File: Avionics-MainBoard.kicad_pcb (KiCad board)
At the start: 4 copper layers, 90.2 x 95.9 mm, 274 parts, among them J1 USB_C_Receptacle_USB2.0, J10 1824543, J11 1824527, J12 1824527, J13 1824527, J14 200528-0100, J15 200528-0100, J16 200528-0100, J17 1824543, J18 200528-0100, J19 200528-0100, J2 200528-0100, J3 Conn_01x06, J4 200528-0100, J5 Micro_SD_Card_Det2, J6 200528-0100, J7 U.FL-R-SMT-1, J8 Conn_01x02, J9 200528-0100, Q1 IRLML2803, Q10 MBT2222ADW1T1, Q11 MBT2222ADW1T1, Q12 MBT2222ADW1T1, Q13 MBT2222ADW1T1, Q14 MMBT2907, Q15 MMBT2907, Q16 NX3008NBKS, Q17 MBT2222ADW1T1, Q18 IRLML0030, Q19 IRF7404, Q2 MBT2222ADW1T1, Q22 NX3008NBKS, Q24 NX3008NBKS, Q26 NX3008NBKS, Q28 NX3008NBKS, Q29 MBT2222ADW1T1, Q3 MBT2222ADW1T1, Q30 MBT2222ADW1T1, Q4 NX3008NBKS, Q44 NX3008NBKS, Q46 NX3008NBKS, Q48 NX3008NBKS, Q5 MBT2222ADW1T1, Q50 NX3008NBKS, Q52 NX3008NBKS, Q6 MBT2222ADW1T1, Q7 MBT2222ADW1T1, Q8 MBT2222ADW1T1, Q9 MBT2222ADW1T1, Q99 NX3008NBKS, SW1 SW_Omron_B3FS, SW2 SW_Omron_B3FS, U1 MR25H40MDF, U12 ADM1491EBR, U14 ADM1176-1ARMZ-R7, U15 TPS7A4501DCQT, U16 ADM1176-1ARMZ-R7, U17 TPS54226PWPR, U18 ADM1176-1ARMZ-R7, U2 RP2040, U3 MAX706RESA+, U4 DS3231S, U5 BNO085, U6 USBLC6-2SC6, U7 E22-900M30S, U8 S1216V8, U9 BQ25883RGER, Y1 12MHz, Y2 32.768kHz

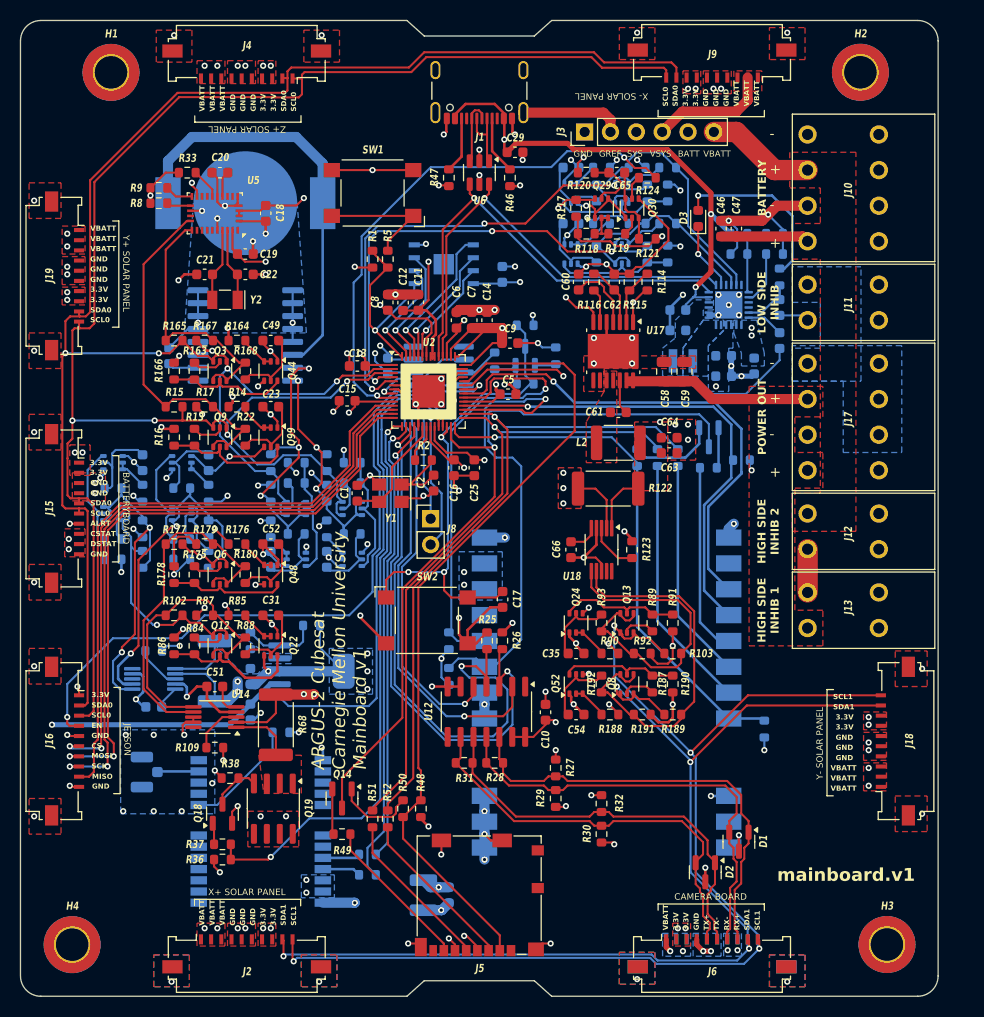
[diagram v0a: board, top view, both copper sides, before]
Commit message: Added better protection to SD card, Jetson IO, and added address breakouts to power monitors
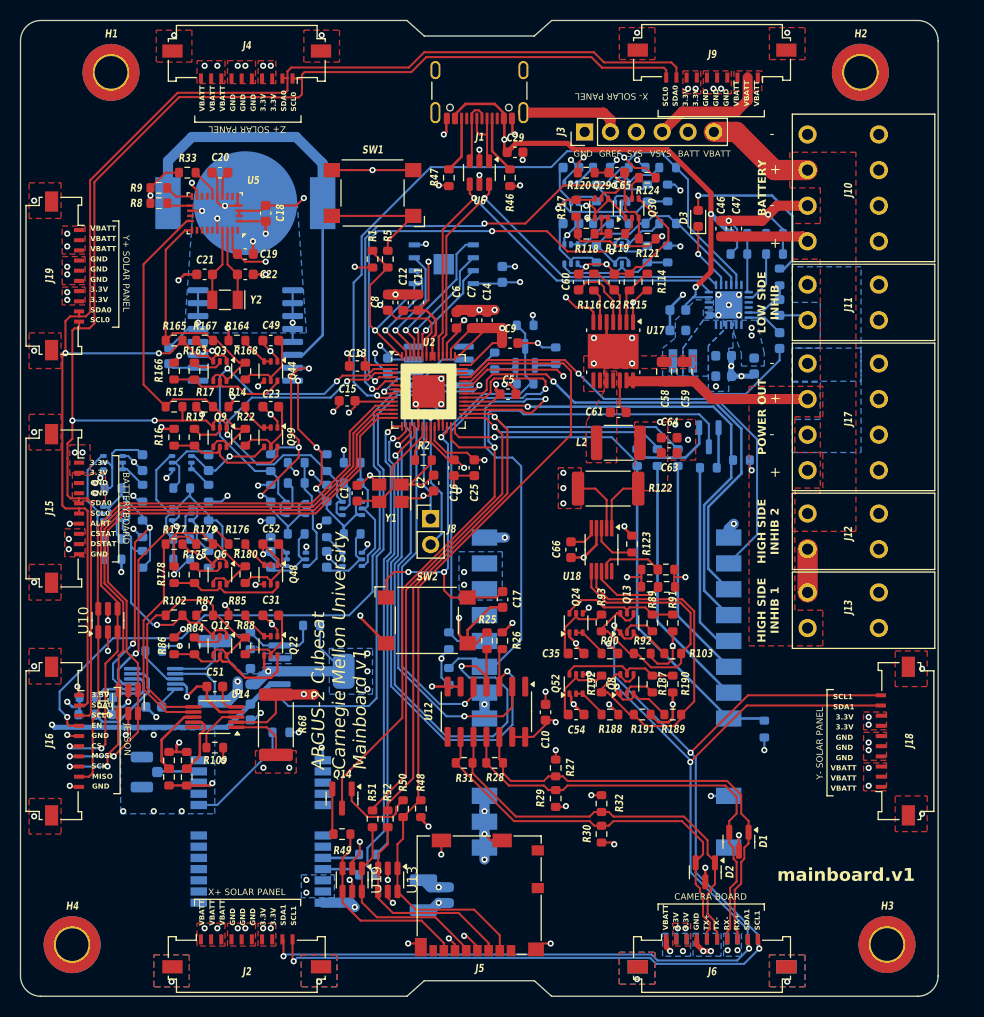
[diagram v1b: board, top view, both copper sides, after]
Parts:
- removed Q18: IRLML0030, Package_TO_SOT_SMD:SOT-23
- removed Q19: IRF7404, Package_SO:SOIC-8_3.9x4.9mm_P1.27mm
- removed R36: 10K, Resistor_SMD:R_0603_1608Metric
- removed R37: 4.7K, Resistor_SMD:R_0603_1608Metric
- removed R38: 3.3K, Resistor_SMD:R_0603_1608Metric
- removed REF**: VAL**, mainboard:board_info_block
- added R39: 0R, Resistor_SMD:R_0603_1608Metric, F.Cu at (168.4, 107.7)
- added R40: 0R, Resistor_SMD:R_0603_1608Metric, F.Cu at (166.7, 107.7)
- added R41: 0R, Resistor_SMD:R_0603_1608Metric, F.Cu at (168.3, 106.0)
- added R42: 0R, Resistor_SMD:R_0603_1608Metric, F.Cu at (166.7, 106.0)
- added R43: 0R, Resistor_SMD:R_0603_1608Metric, B.Cu at (113.2, 118.6)
- added R44: 0R, Resistor_SMD:R_0603_1608Metric, B.Cu at (111.5, 118.6)
- added R45: 0R, Resistor_SMD:R_0603_1608Metric, B.Cu at (113.1, 120.2)
- added R53: 0R, Resistor_SMD:R_0603_1608Metric, B.Cu at (111.4, 120.2)
- added R54: 0R, Resistor_SMD:R_0603_1608Metric, F.Cu at (119.5, 124.8)
- added R64: 0R, Resistor_SMD:R_0603_1608Metric, F.Cu at (119.5, 126.4)
- added R71: 0R, Resistor_SMD:R_0603_1608Metric, F.Cu at (121.2, 124.8)
- added R72: 0R, Resistor_SMD:R_0603_1608Metric, F.Cu at (121.2, 126.4)
- added U10: USBLC6-2SC6, Package_TO_SOT_SMD:SOT-23-6, F.Cu at (113.5, 111.0)
- added U11: USBLC6-2SC6, Package_TO_SOT_SMD:SOT-23-6, F.Cu at (115.5, 119.0)
- added U13: USBLC6-2SC6, Package_TO_SOT_SMD:SOT-23-6, F.Cu at (141.0, 136.5)
- added U19: USBLC6-2SC6, Package_TO_SOT_SMD:SOT-23-6, F.Cu at (137.5, 136.5)
- L2: value 3.3uH -> +3V3uH
- moved R123 0.55 mm to (165.0, 103.5)
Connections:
- J10 pad 5: GNDREF -> unconnected-(J10-Pad5)_1
- J10 pad 6: GNDREF -> unconnected-(J10-Pad6)_1
- J11 pad 3: GNDREF -> unconnected-(J11-MP-Pad3)
- J11 pad 4: GNDREF -> unconnected-(J11-MP-Pad4)
- J12 pad 3: GND -> unconnected-(J12-MP-Pad3)
- J12 pad 4: GND -> unconnected-(J12-MP-Pad4)
- J13 pad 3: GND -> unconnected-(J13-MP-Pad3)
- J13 pad 4: GND -> unconnected-(J13-MP-Pad4)
- J17 pad 5: GND -> unconnected-(J17-Pad5)
- J17 pad 6: GND -> unconnected-(J17-Pad6)_1
- R68 pad 2: Net-(U14-VCC) -> +3V3
- U14 pad 1: Net-(U14-VCC) -> +3V3
- U14 pad 8: GND -> /GPS Power/A0
- U14 pad 9: GND -> /GPS Power/A1
- U16 pad 8: unconnected-(U16-A0-Pad8) -> /LoRa Power/A0
- U16 pad 9: GND -> /LoRa Power/A1
- U18 pad 8: GND -> /Main Power/A0
- U18 pad 9: unconnected-(U18-A1-Pad9) -> /Main Power/A1
- U2 pad 39: /MCU_IO/GPS_EN -> /LoRa Power/LoRa_INT
- U7 pad 13: unconnected-(U7-DIO1-Pad13) -> /LoRa Power/LoRa_INT
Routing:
- net /MCU_IO/GPS_EN: track 70.1 -> 0.00 mm, vias 2 -> 0
- net /LoRa Power/LoRa_INT: track 0.00 -> 46.1 mm, vias 0 -> 1
- net GNDREF: track 45.8 -> 67.4 mm
- net +3V3: track 167.0 -> 186.2 mm, vias 76 -> 81
- net /LoRa Power/A1: track 0.00 -> 9.85 mm
- net /LoRa Power/A0: track 0.00 -> 7.38 mm
- net /Main Power/A0: track 0.00 -> 7.35 mm
- net /GPS Power/A0: track 0.00 -> 7.19 mm
- net GND: track 320.8 -> 327.8 mm, vias 129 -> 131
- net /Main Power/A1: track 0.00 -> 6.44 mm
- net /GPS Power/A1: track 0.00 -> 6.24 mm
- net Net-(U14-VCC): track 6.08 -> 0.00 mm
- net /SD/SD_MOSI: track 16.2 -> 21.3 mm
- net Net-(Q18-D): track 4.95 -> 0.00 mm
- net /SD/SD_CLK: track 15.7 -> 20.3 mm
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- removed copper zone on F.Cu, net Net-(U14-VCC)

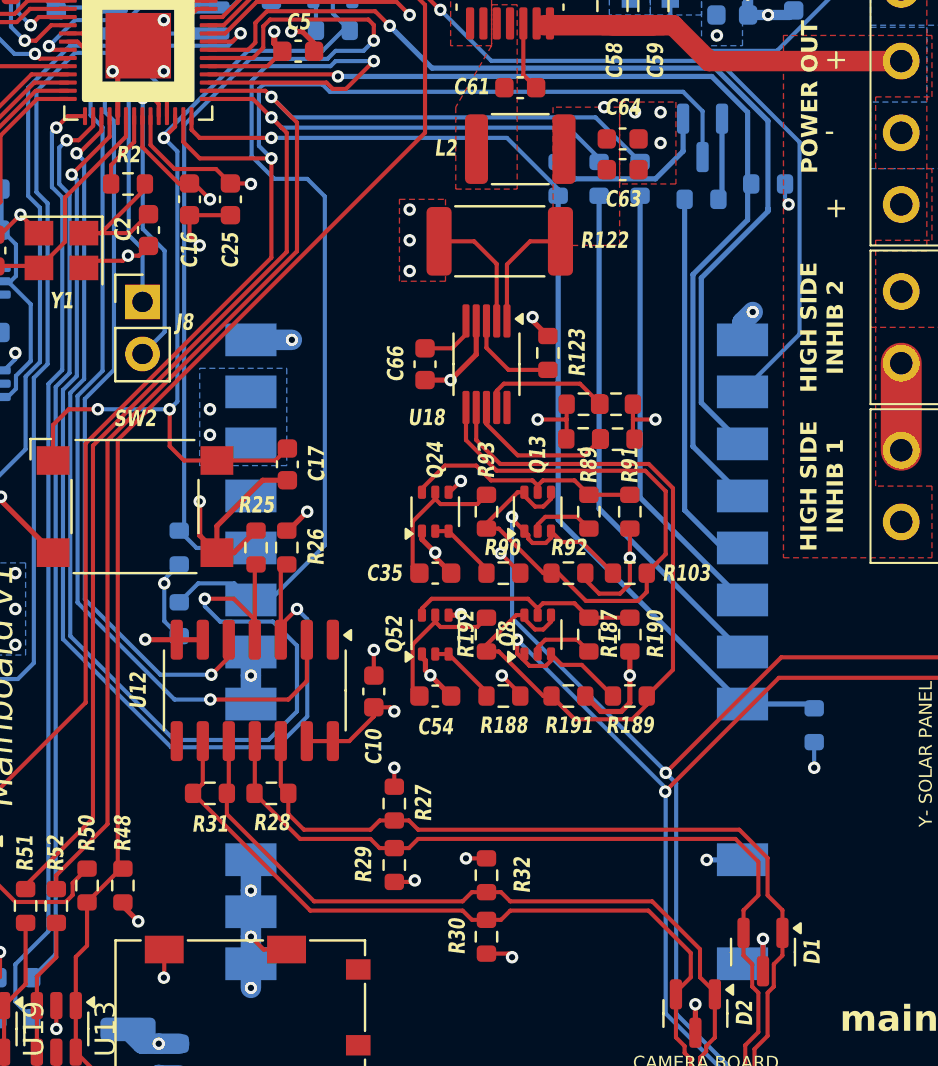
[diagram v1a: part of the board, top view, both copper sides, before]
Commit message: Added extra decoupling caps to LoRa
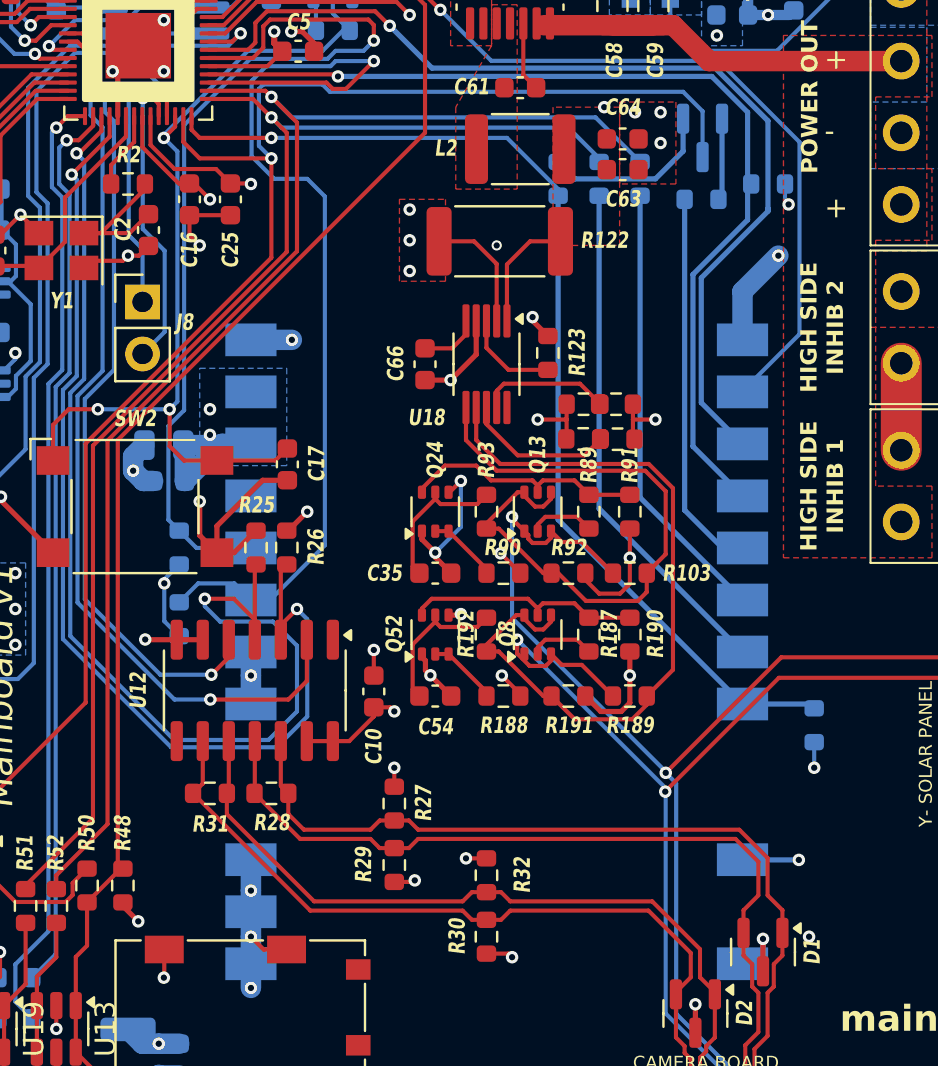
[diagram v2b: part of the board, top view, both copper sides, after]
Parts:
- added C26: 1u, Capacitor_SMD:C_0603_1608Metric, B.Cu at (146.5, 109.8)
- added C27: 10u, Capacitor_SMD:C_0805_2012Metric, B.Cu at (146.2, 108.0)
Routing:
- net GND: track 327.8 -> 419.8 mm, vias 131 -> 134
- net LoRa_VDD: track 47.9 -> 57.0 mm
- net /LoRa Power/LoRa_TX_EN: track 44.7 -> 45.5 mm

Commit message: Updated version to v2.1
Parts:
- turned H3 to 180 degrees
- turned H4 to 180 degrees
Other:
- board text added: "ARGUS-2 Cubesat Carnegie Mellon University Mainboard v2.1"
- board text added: "mainboard.v2.1"
- board text removed: "ARGUS-2 Cubesat Carnegie Mellon University Mainboard v1"
- board text removed: "mainboard.v1"

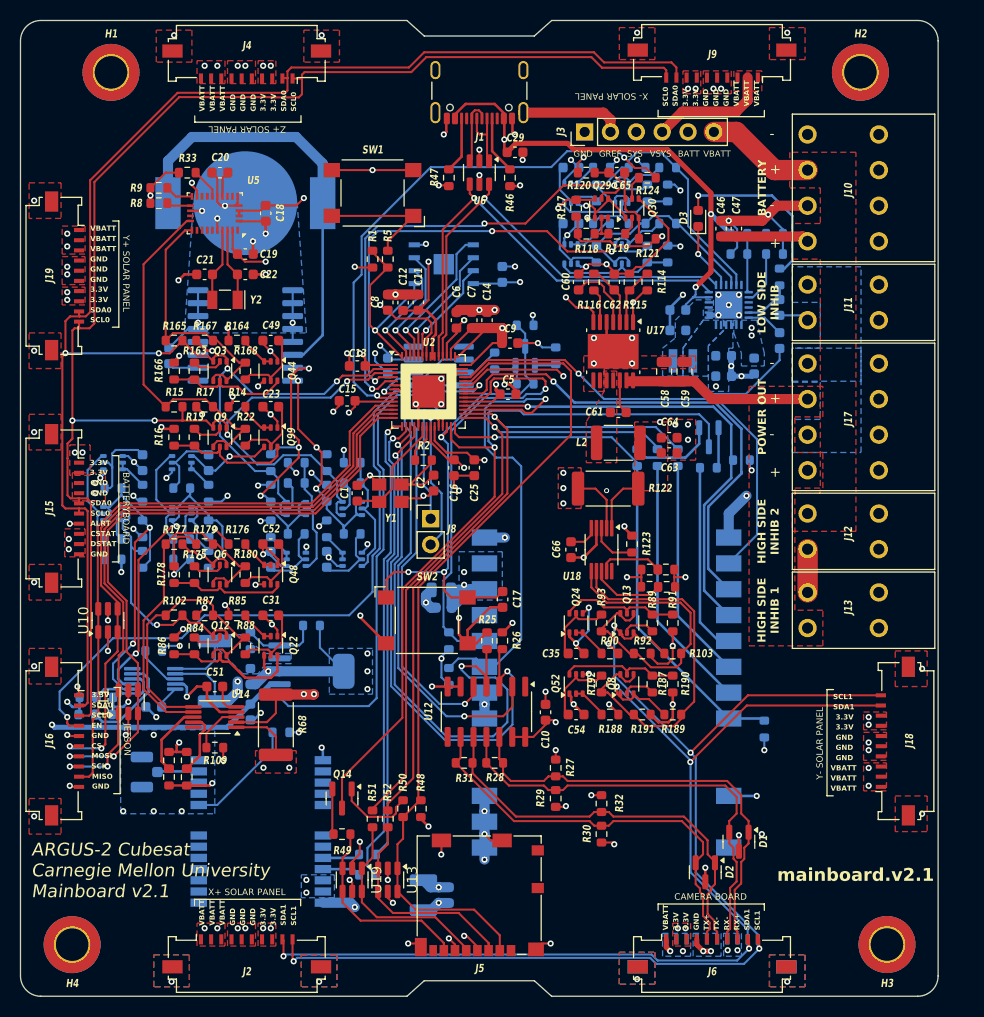
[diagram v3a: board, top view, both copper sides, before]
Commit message: Updated IMU layout
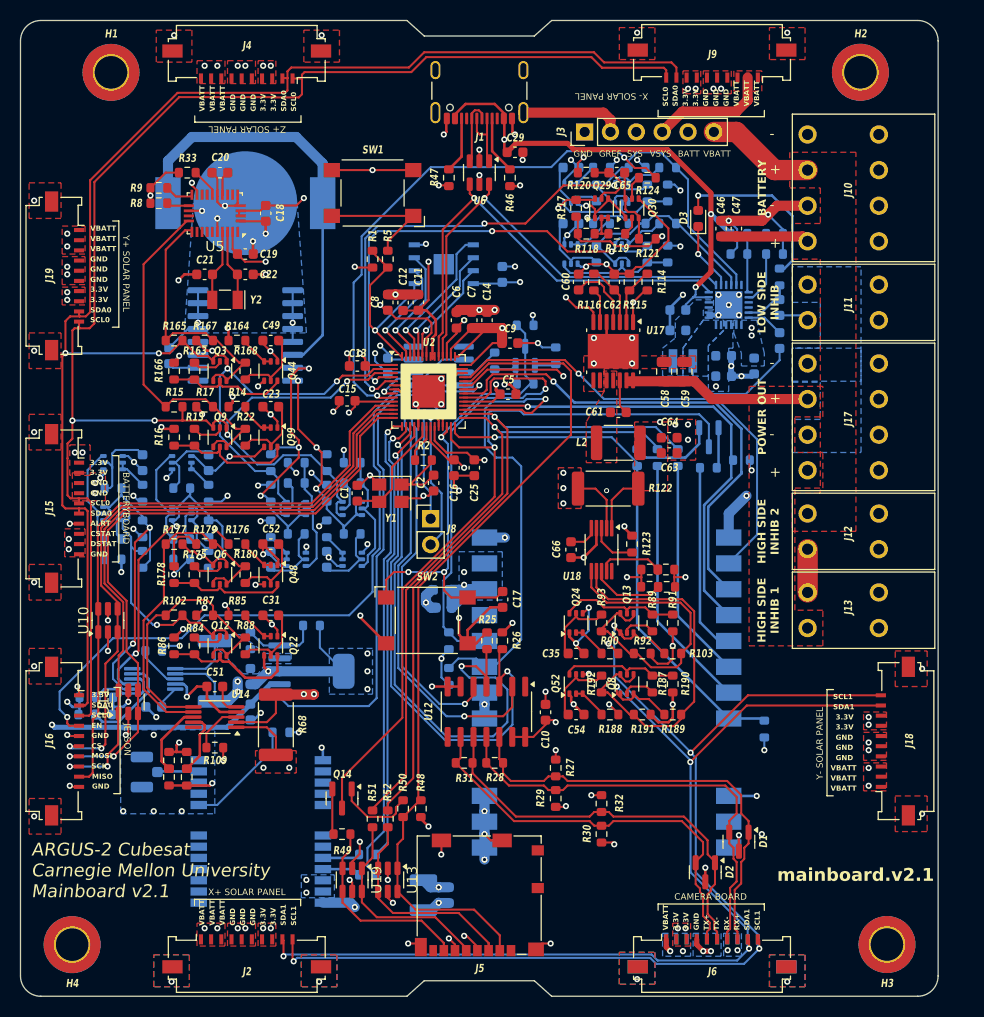
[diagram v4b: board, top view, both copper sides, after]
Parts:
- C27: value 10u -> 1u; footprint Capacitor_SMD:C_0805_2012Metric -> Capacitor_SMD:C_0603_1608Metric
- U5: footprint Package_LGA:LGA-28_5.2x3.8mm_P0.5mm -> Argus-IC:BNO085
